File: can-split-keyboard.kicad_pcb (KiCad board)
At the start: 2 copper layers, 14 x 14 mm, 90 parts, among them SW1 SW_Push, SW10 SW_Push, SW11 SW_Push, SW12 SW_Push, SW13 SW_Push, SW14 SW_Push, SW15 SW_Push, SW16 SW_Push, SW17 SW_Push, SW18 SW_Push, SW19 SW_Push, SW2 SW_Push, SW20 SW_Push, SW21 SW_Push, SW22 SW_Push, SW23 SW_Push, SW24 SW_Push, SW25 SW_Push, SW26 SW_Push, SW27 SW_Push, SW28 SW_Push, SW29 SW_Push, SW3 SW_Push, SW30 SW_Push, SW31 SW_Push, SW32 SW_Push, SW33 SW_Push, SW34 SW_Push, SW35 SW_Push, SW36 SW_Push, SW37 SW_Push, SW38 SW_Push, SW39 SW_Push, SW4 SW_Push, SW40 SW_Push, SW41 SW_Push, SW42 SW_Push, SW5 SW_Push, SW6 SW_Push, SW7 SW_Push, SW8 SW_Push, SW9 SW_Push

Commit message: Placed all the switches on PCB.
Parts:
- SW12, SW36: footprint Peej Footprints:MX_CUTOUT -> Peej Footprints:MX
- SW42, SW6: footprint Peej Footprints:MX_CUTOUT -> Peej Footprints:MX2U_CUTOUT
- moved SW4 192.6 mm to (47.0, 91.4)
- moved SW1 178.1 mm to (47.0, 34.3)
- moved SW8 171.8 mm to (66.0, 53.3)
- moved SW2 159.3 mm to (47.0, 53.3)
- moved SW5 153.7 mm to (47.0, 110.5)
- moved D27 152.4 mm to (269.5, 141.8)
- moved D29 152.4 mm to (269.5, 138.3)
- moved D31 152.4 mm to (269.5, 134.7)
- moved D33 152.4 mm to (269.5, 131.2)
- moved D1 152.4 mm to (202.7, 138.6)
- moved D14 152.4 mm to (312.6, 138.3)
- moved D16 152.4 mm to (312.6, 134.7)
- moved D17 152.4 mm to (312.6, 131.2)
- moved D20 152.4 mm to (280.2, 141.8)
- moved D22 152.4 mm to (202.7, 142.1)
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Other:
- board size 14 x 14 mm -> 33 x 14 mm

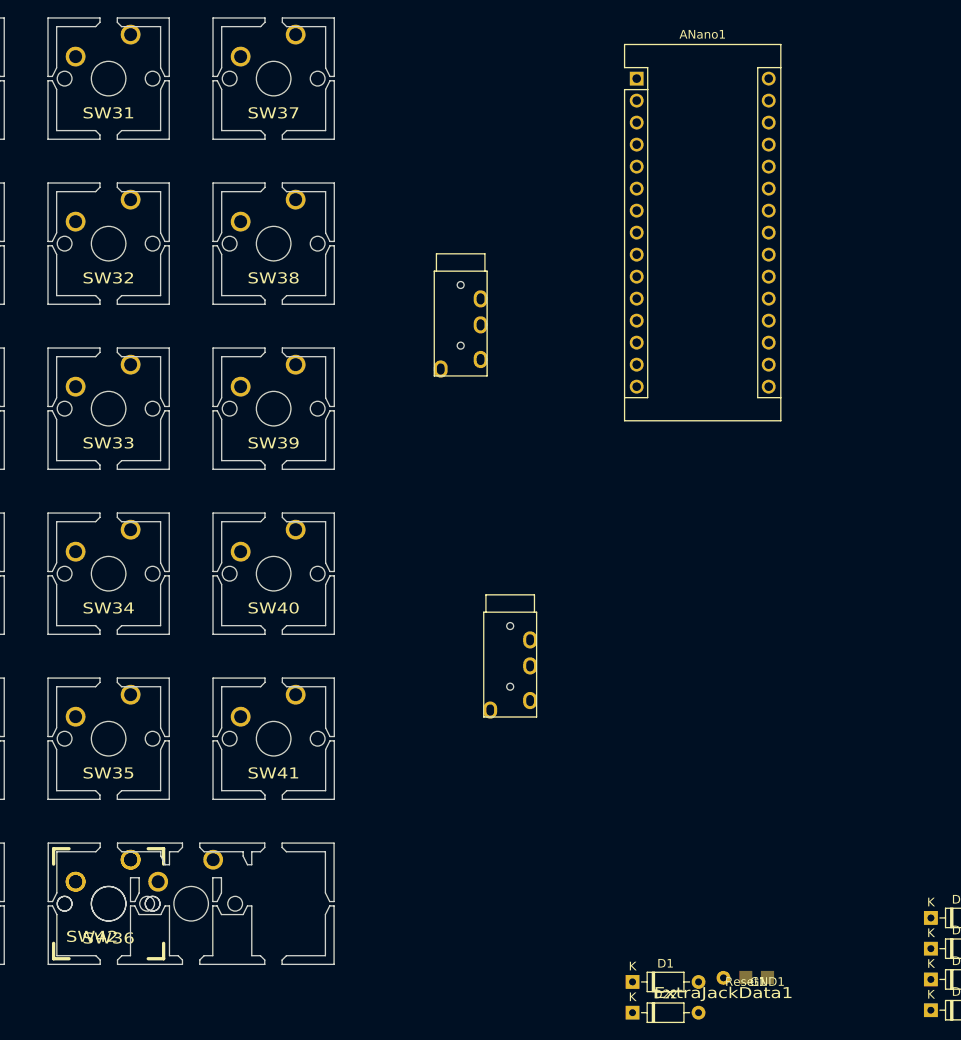
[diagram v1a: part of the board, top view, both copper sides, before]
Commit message: Fixed right buttom corner double key.
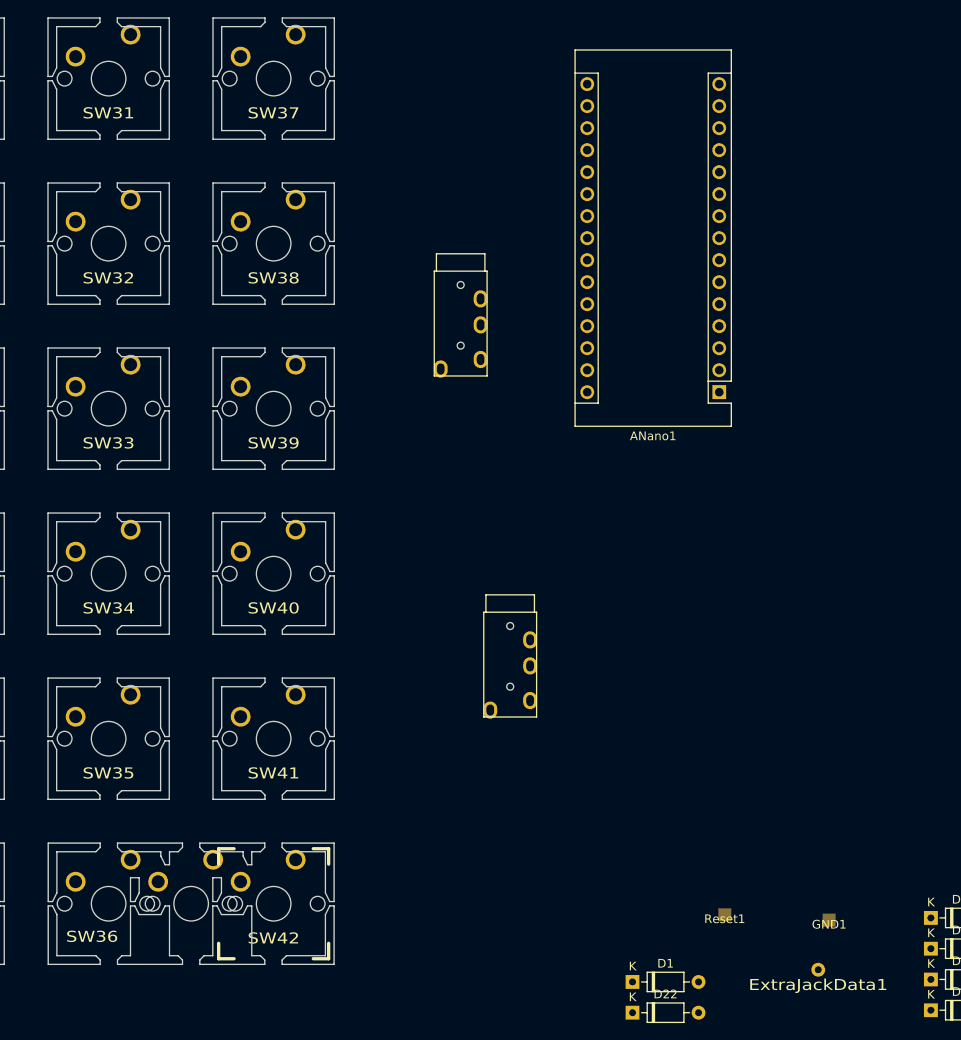
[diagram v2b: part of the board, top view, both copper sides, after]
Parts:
- SW36: footprint Peej Footprints:MX -> Peej Footprints:MX2U_CUTOUT
- SW42: footprint Peej Footprints:MX2U_CUTOUT -> Peej Footprints:MX
- moved ANano1 37.4 mm to (212.7, 70.5), turned to 180 degrees
- moved ExtraJackData1 11.0 mm to (224.2, 137.2)
- moved GND1 9.72 mm to (225.4, 131.4)
- moved SW42 9.53 mm to (161.3, 129.5)
- moved SW36 9.52 mm to (151.8, 129.5)
- moved Reset1 7.64 mm to (213.4, 130.8)

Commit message: Placed Microcontroller, jacks, and outer edge cut.
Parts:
- moved Jack2 149.1 mm to (56.5, 26.7)
- moved D11 114.5 mm to (202.2, 50.7)
- moved D12 114.5 mm to (182.3, 70.6)
- moved D10 114.5 mm to (222.2, 30.7)
- moved D4 114.5 mm to (182.3, 74.2)
- moved D5 114.5 mm to (202.2, 54.2)
- moved D6 114.5 mm to (226.1, 39.4)
- moved D20 102.4 mm to (201.5, 76.4)
- moved D8 102.4 mm to (233.8, 76.4)
- moved D13 102.4 mm to (223.0, 76.4)
- moved D14 102.4 mm to (233.8, 72.9)
- moved D17 102.4 mm to (233.8, 65.8)
- moved D19 102.4 mm to (212.3, 76.4)
- moved D3 102.4 mm to (201.5, 72.9)
- moved D32 102.4 mm to (201.5, 65.8)
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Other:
- board size 33 x 14 mm -> 133.3 x 114.3 mm

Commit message: Placed everything.
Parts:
- moved D6 191.2 mm to (52.7, 120.0), turned to 180 degrees
- moved D7 174.7 mm to (71.8, 43.8), turned to 180 degrees
- moved D9 173.6 mm to (71.8, 81.9), turned to 180 degrees
- moved D10 166.0 mm to (71.8, 101.0), turned to 180 degrees
- moved D8 162.6 mm to (71.8, 62.9), turned to 180 degrees
- moved ExtraJackData1 162.4 mm to (75.6, 29.8)
- moved D2 159.7 mm to (52.7, 62.9), turned to 180 degrees
- moved D5 157.6 mm to (56.5, 114.3), turned to 90 degrees
- moved D3 149.1 mm to (52.7, 81.9), turned to 180 degrees
- moved D17 147.4 mm to (94.6, 114.3), turned to 90 degrees
- moved D16 146.5 mm to (90.8, 101.0), turned to 180 degrees
- moved D14 143.4 mm to (90.8, 62.9), turned to 180 degrees
- moved D11 141.7 mm to (75.6, 114.3), turned to 90 degrees
- moved D18 141.6 mm to (90.8, 120.0), turned to 180 degrees
- moved D13 136.2 mm to (90.8, 43.8), turned to 180 degrees
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
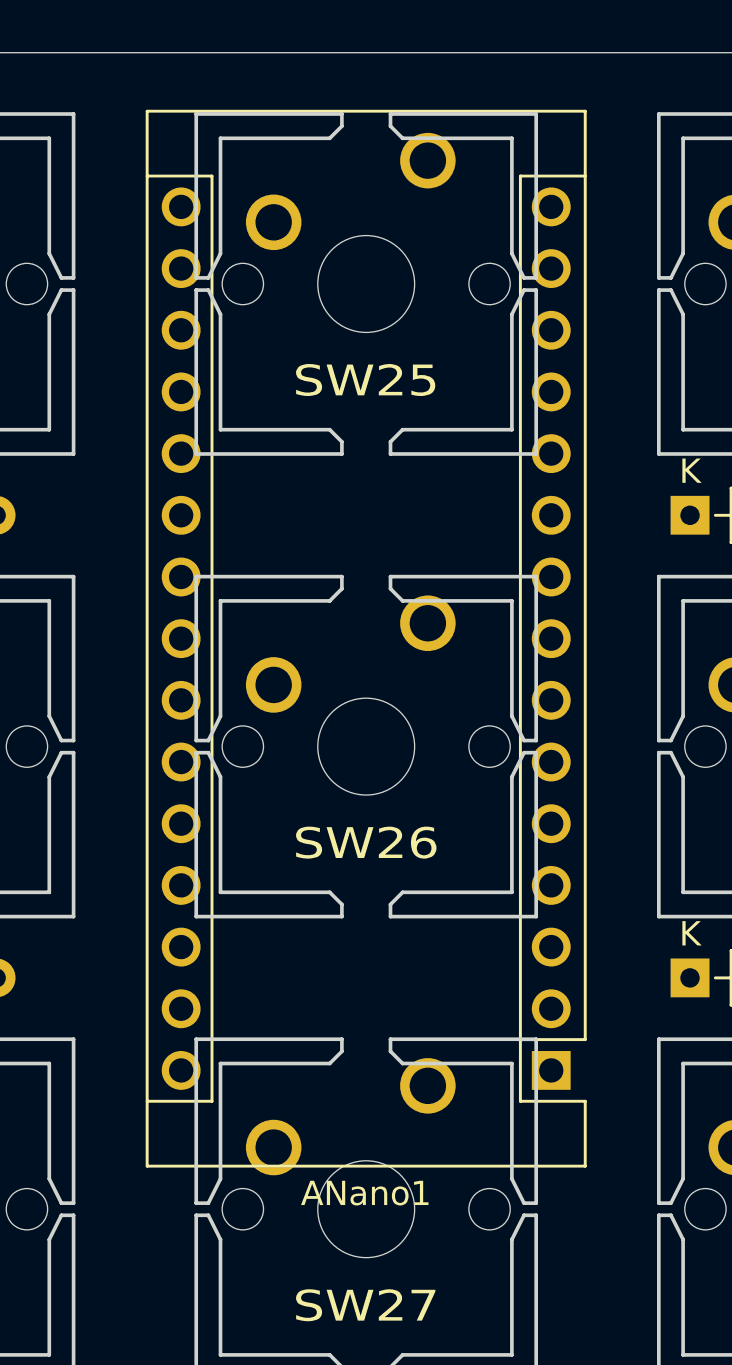
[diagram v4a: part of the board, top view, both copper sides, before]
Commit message: Put arduino to the other side of the PCB. Changed track clearence to 0.25mm.
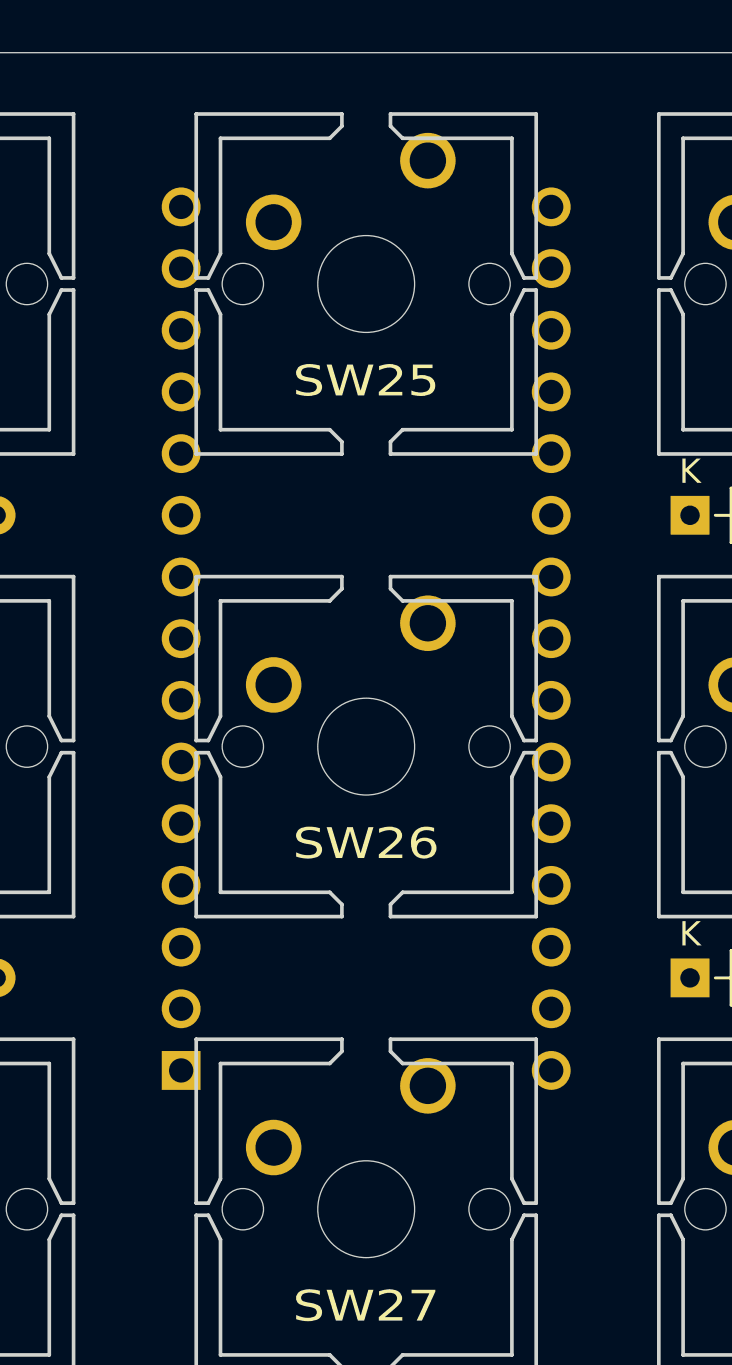
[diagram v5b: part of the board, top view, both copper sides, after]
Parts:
- ANano1: moved to B.Cu
- moved ANano1 15.2 mm to (115.6, 66.7), turned to 0 degrees
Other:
- net class Default: clearance 0.2 -> 0.25
- rule trace_clearance: 0.2 -> 0.25

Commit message: Placed all the tracks.
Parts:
- moved D25 7.88 mm to (108.2, 43.7), turned to 180 degrees
- moved D26 7.88 mm to (108.2, 63.0), turned to 180 degrees
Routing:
- net GND: track 0.00 -> 441.4 mm, vias 0 -> 10
- net /Data: track 0.00 -> 278.7 mm, vias 0 -> 6
- net VCC: track 0.00 -> 277.1 mm, vias 0 -> 11
- net /Col0: track 0.00 -> 217.4 mm
- net /Col1: track 0.00 -> 198.4 mm, vias 0 -> 2
- net /Row5: track 0.00 -> 195.0 mm
- net /Row4: track 0.00 -> 191.9 mm
- net /Col2: track 0.00 -> 182.1 mm, vias 0 -> 1
- net /Row1: track 0.00 -> 176.5 mm
- net /Row3: track 0.00 -> 173.3 mm
- net /Col3: track 0.00 -> 162.1 mm, vias 0 -> 1
- net /Row2: track 0.00 -> 156.6 mm
- net /Col6: track 0.00 -> 148.6 mm
- net /Col5: track 0.00 -> 141.5 mm
- net /Row0: track 0.00 -> 132.2 mm
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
